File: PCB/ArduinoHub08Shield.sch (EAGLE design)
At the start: 2 parts

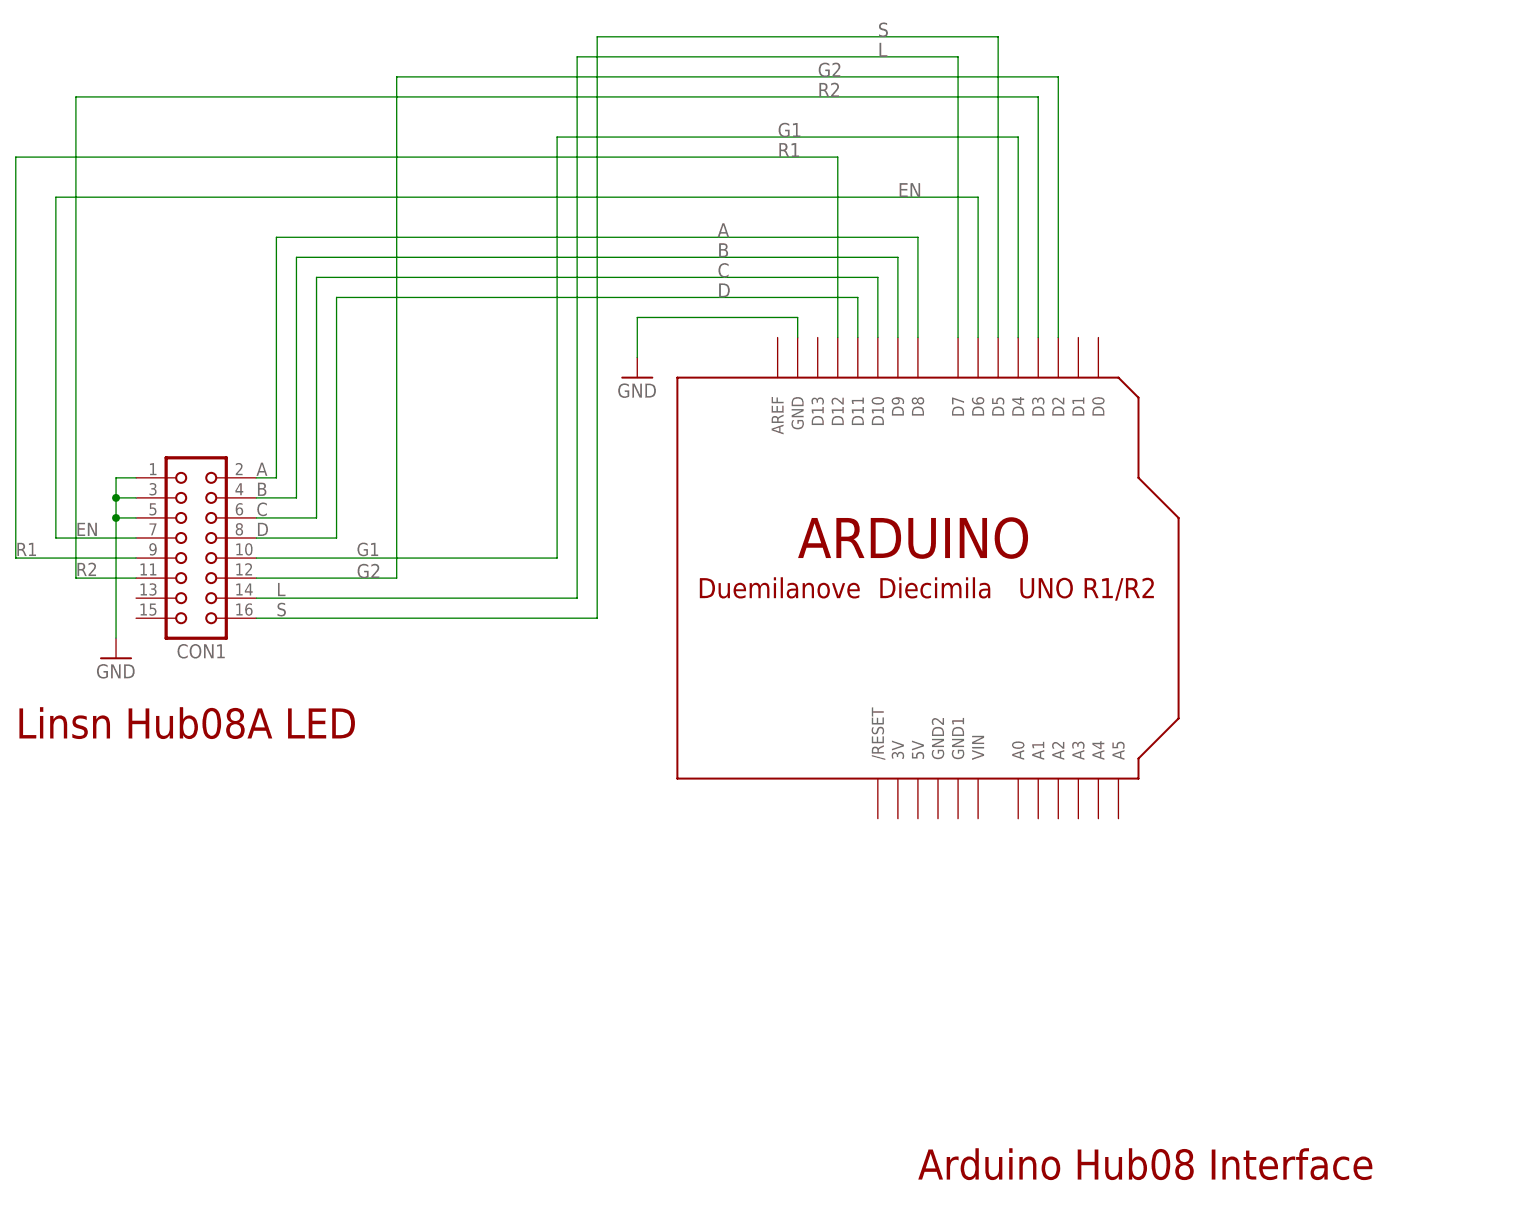
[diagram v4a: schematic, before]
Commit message: PCB/schematic update: LDR light sensor added
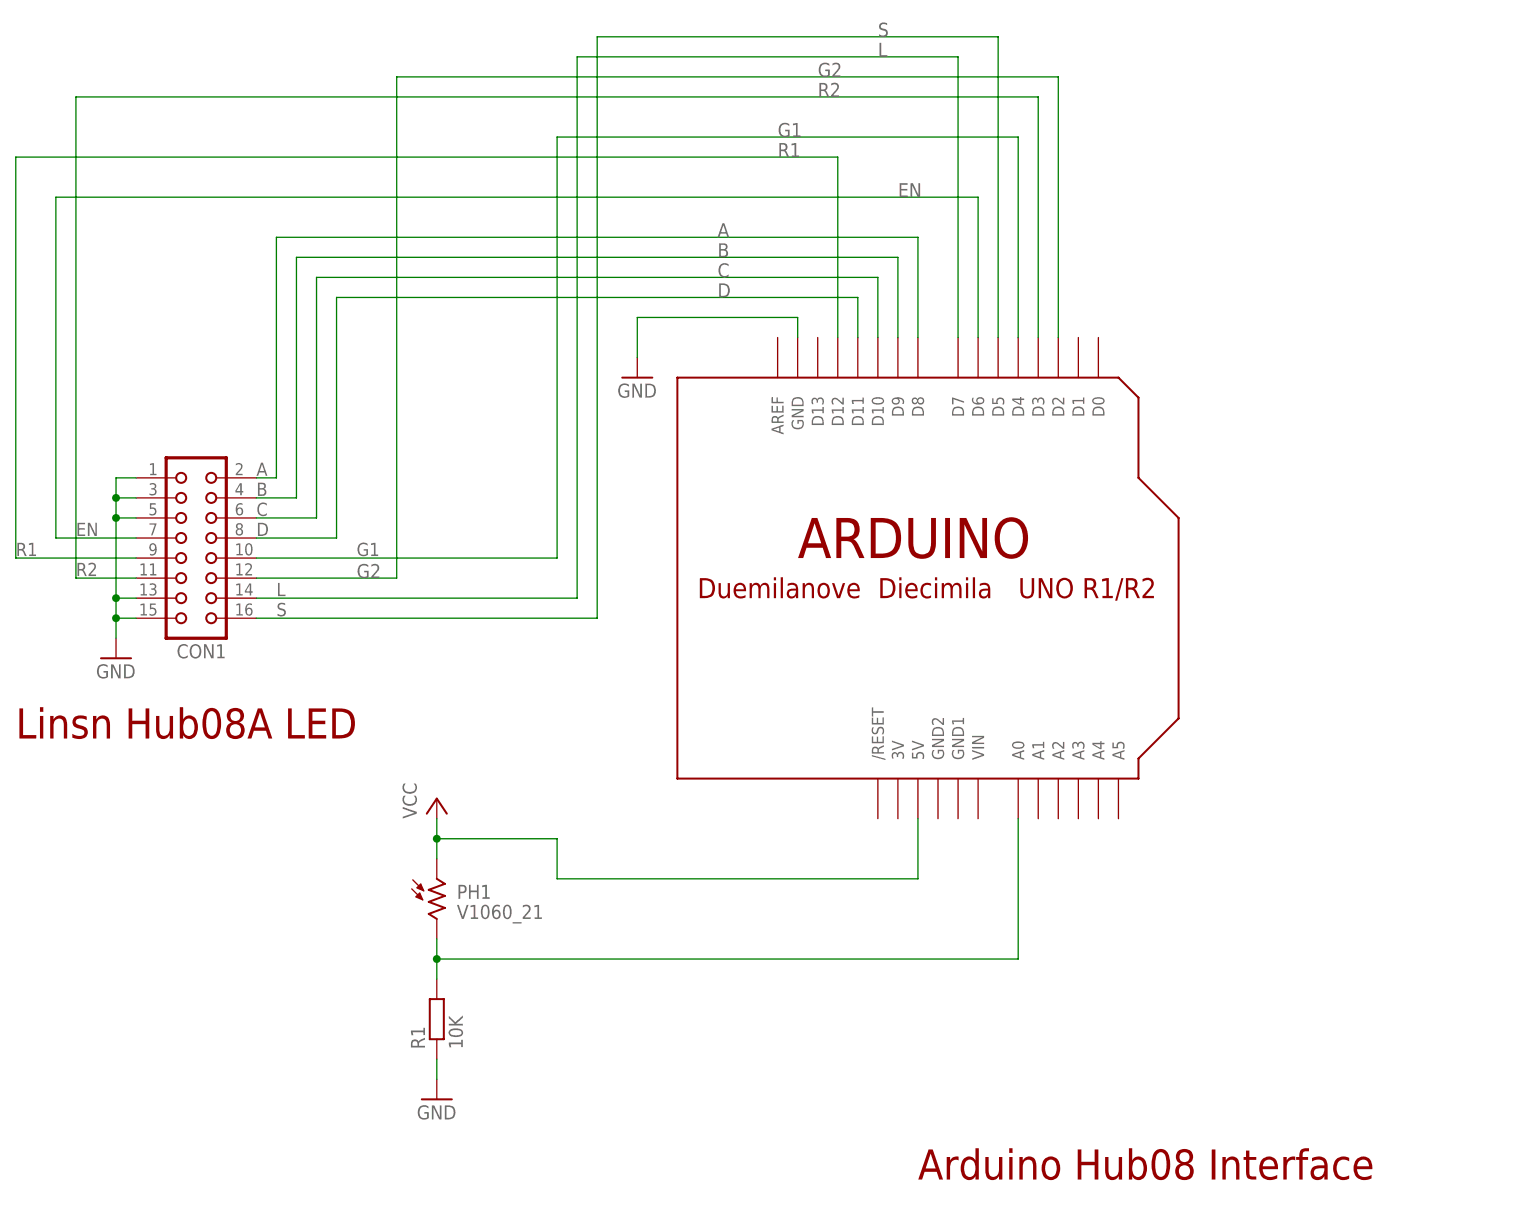
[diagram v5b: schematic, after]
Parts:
- added PH1: V1060_21, photo-elements:V1060_21
- added R1: 10K, rcl:R-EU_0204/7
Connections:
- new net N$1: PH1.2, R1.2, U$1.A0
- new net VCC: PH1.1, U$1.5V
- net GND: now also CON1.13, CON1.15, R1.1
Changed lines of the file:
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@@
 <grid distance="0.1" unitdist="inch" unit="inch" style="lines" multiple="1" display="no" altdistance="0.01" altunitdist="inch" altunit="inch"/>
 <layers>
-<layer number="1" name="Top" color="4" fill="1" visible="no" active="no"/>
-<layer number="16" name="Bottom" color="1" fill="1" visible="no" active="no"/>
-<layer number="17" name="Pads" color="2" fill="1" visible="no" active="no"/>
-<layer number="18" name="Vias" color="2" fill="1" visible="no" active="no"/>
-<layer number="19" name="Unrouted" color="6" fill="1" visible="no" active="no"/>
-<layer number="20" name="Dimension" color="15" fill="1" visible="no" active="no"/>
-<layer number="21" name="tPlace" color="7" fill="1" visible="no" active="no"/>
-<layer number="22" name="bPlace" color="7" fill="1" visible="no" active="no"/>
-<layer number="23" name="tOrigins" color="15" fill="1" visible="no" active="no"/>
-<layer number="24" name="bOrigins" color="15" fill="1" visible="no" active="no"/>
-<layer number="25" name="tNames" color="7" fill="1" visible="no" active="no"/>
-<layer number="26" name="bNames" color="7" fill="1" visible="no" active="no"/>
-<layer number="27" name="tValues" color="7" fill="1" visible="no" active="no"/>
-<layer number="28" name="bValues" color="7" fill="1" visible="no" active="no"/>
+<layer number="1" name="Top" color="4" fill="1" visible="yes" active="no"/>
+<layer number="16" name="Bottom" color="1" fill="1" visible="yes" active="no"/>
+<layer number="17" name="Pads" color="2" fill="1" visible="yes" active="no"/>
+<layer number="18" name="Vias" color="2" fill="1" visible="yes" active="no"/>
+<layer number="19" name="Unrouted" color="6" fill="1" visible="yes" active="no"/>
+<layer number="20" name="Dimension" color="15" fill="1" visible="yes" active="no"/>
+<layer number="21" name="tPlace" color="7" fill="1" visible="yes" active="no"/>
+<layer number="22" name="bPlace" color="7" fill="1" visible="yes" active="no"/>
+<layer number="23" name="tOrigins" color="15" fill="1" visible="yes" active="no"/>
+<layer number="24" name="bOrigins" color="15" fill="1" visible="yes" active="no"/>
+<layer number="25" name="tNames" color="7" fill="1" visible="yes" active="no"/>
+<layer number="26" name="bNames" color="7" fill="1" visible="yes" active="no"/>
+<layer number="27" name="tValues" color="7" fill="1" visible="yes" active="no"/>
+<layer number="28" name="bValues" color="7" fill="1" visible="yes" active="no"/>
 <layer number="29" name="tStop" color="7" fill="3" visible="no" active="no"/>
 <layer number="30" name="bStop" color="7" fill="6" visible="no" active="no"/>
@@
 <layer number="35" name="tGlue" color="7" fill="4" visible="no" active="no"/>
 <layer number="36" name="bGlue" color="7" fill="5" visible="no" active="no"/>
-<layer number="37" name="tTest" color="7" fill="1" visible="no" active="no"/>
-<layer number="38" name="bTest" color="7" fill="1" visible="no" active="no"/>
+<layer number="37" name="tTest" color="7" fill="1" visible="yes" active="no"/>
+<layer number="38" name="bTest" color="7" fill="1" visible="yes" active="no"/>
 <layer number="39" name="tKeepout" color="4" fill="11" visible="no" active="no"/>
 <layer number="40" name="bKeepout" color="1" fill="11" visible="no" active="no"/>
@@
 <layer number="44" name="Drills" color="7" fill="1" visible="no" active="no"/>
 <layer number="45" name="Holes" color="7" fill="1" visible="no" active="no"/>
-<layer number="46" name="Milling" color="3" fill="1" visible="no" active="no"/>
-<layer number="47" name="Measures" color="7" fill="1" visible="no" active="no"/>
-<layer number="48" name="Document" color="7" fill="1" visible="no" active="no"/>
-<layer number="49" name="Reference" color="7" fill="1" visible="no" active="no"/>
-<layer number="50" name="dxf" color="7" fill="1" visible="no" active="no"/>
-<layer number="51" name="tDocu" color="7" fill="1" visible="no" active="no"/>
-<layer number="52" name="bDocu" color="7" fill="1" visible="no" active="no"/>
-<layer number="53" name="tGND_GNDA" color="7" fill="9" visible="no" active="no"/>
-<layer number="54" name="bGND_GNDA" color="1" fill="9" visible="no" active="no"/>
-<layer number="56" name="wert" color="7" fill="1" visible="no" active="no"/>
-<layer number="57" name="tCAD" color="7" fill="1" visible="no" active="no"/>
+<layer number="46" name="Milling" color="3" fill="1" visible="yes" active="no"/>
+<layer number="47" name="Measures" color="7" fill="1" visible="yes" active="no"/>
+<layer number="48" name="Document" color="7" fill="1" visible="yes" active="no"/>
+<layer number="49" name="Reference" color="7" fill="1" visible="yes" active="no"/>
+<layer number="50" name="dxf" color="7" fill="1" visible="yes" active="no"/>
+<layer number="51" name="tDocu" color="7" fill="1" visible="yes" active="no"/>
+<layer number="52" name="bDocu" color="7" fill="1" visible="yes" active="no"/>
+<layer number="53" name="tGND_GNDA" color="7" fill="9" visible="yes" active="no"/>
+<layer number="54" name="bGND_GNDA" color="1" fill="9" visible="yes" active="no"/>
+<layer number="56" name="wert" color="7" fill="1" visible="yes" active="no"/>
+<layer number="57" name="tCAD" color="7" fill="1" visible="yes" active="no"/>
 <layer number="90" name="Modules" color="5" fill="1" visible="yes" active="yes"/>
 <layer number="91" name="Nets" color="2" fill="1" visible="yes" active="yes"/>
@@
 <part name="GND1" library="supply1" deviceset="GND" device=""/>
 <part name="GND2" library="supply1" deviceset="GND" device=""/>
+<part name="GND3" library="supply1" deviceset="GND" device=""/>
+<part name="P+1" library="supply1" deviceset="VCC" device=""/>
+<part name="R1" library="rcl" deviceset="R-EU_" device="0204/7" value="10K"/>
+<part name="PH1" library="photo-elements" deviceset="?1060*" device="V" technology="_21"/>
 </parts>
 <sheets>
@@
 <instance part="GND1" gate="1" x="73.66" y="93.98"/>
 <instance part="GND2" gate="1" x="139.7" y="129.54"/>
+<instance part="GND3" gate="1" x="114.3" y="38.1"/>
+<instance part="P+1" gate="VCC" x="114.3" y="76.2"/>
+<instance part="R1" gate="G$1" x="114.3" y="48.26" rot="R90"/>
+<instance part="PH1" gate="G$1" x="114.3" y="63.5"/>
 </instances>
 <busses>
@@
 <pinref part="GND1" gate="1" pin="GND"/>
 <pinref part="CON1" gate="G$1" pin="1"/>
-<wire x1="73.66" y1="96.52" x2="73.66" y2="111.76" width="0.1524" layer="91"/>
+<wire x1="73.66" y1="96.52" x2="73.66" y2="99.06" width="0.1524" layer="91"/>
+<wire x1="73.66" y1="99.06" x2="73.66" y2="101.6" width="0.1524" layer="91"/>
+<wire x1="73.66" y1="101.6" x2="73.66" y2="111.76" width="0.1524" layer="91"/>
 <wire x1="73.66" y1="111.76" x2="73.66" y2="114.3" width="0.1524" layer="91"/>
 <wire x1="73.66" y1="114.3" x2="73.66" y2="116.84" width="0.1524" layer="91"/>
@@
 <wire x1="73.66" y1="111.76" x2="76.2" y2="111.76" width="0.1524" layer="91"/>
 <junction x="73.66" y="111.76"/>
+<pinref part="CON1" gate="G$1" pin="13"/>
+<wire x1="73.66" y1="101.6" x2="76.2" y2="101.6" width="0.1524" layer="91"/>
+<junction x="73.66" y="101.6"/>
+<pinref part="CON1" gate="G$1" pin="15"/>
+<wire x1="73.66" y1="99.06" x2="76.2" y2="99.06" width="0.1524" layer="91"/>
+<junction x="73.66" y="99.06"/>
 </segment>
 <segment>
@@
 <pinref part="U$1" gate="G$1" pin="GND"/>
 <wire x1="160.02" y1="137.16" x2="160.02" y2="134.62" width="0.1524" layer="91"/>
+</segment>
+<segment>
+<pinref part="GND3" gate="1" pin="GND"/>
+<wire x1="114.3" y1="43.18" x2="114.3" y2="40.64" width="0.1524" layer="91"/>
+<pinref part="R1" gate="G$1" pin="1"/>
 </segment>
 </net>
@@
 </segment>
 </net>
+<net name="N$1" class="0">
+<segment>
+<wire x1="114.3" y1="58.42" x2="114.3" y2="55.88" width="0.1524" layer="91"/>
+<pinref part="U$1" gate="G$1" pin="A0"/>
+<wire x1="114.3" y1="55.88" x2="114.3" y2="53.34" width="0.1524" layer="91"/>
+<wire x1="114.3" y1="55.88" x2="187.96" y2="55.88" width="0.1524" layer="91"/>
+<wire x1="187.96" y1="55.88" x2="187.96" y2="73.66" width="0.1524" layer="91"/>
+<junction x="114.3" y="55.88"/>
+<pinref part="R1" gate="G$1" pin="2"/>
+<pinref part="PH1" gate="G$1" pin="2"/>
+</segment>
+</net>
+<net name="VCC" class="0">
+<segment>
+<pinref part="P+1" gate="VCC" pin="VCC"/>
+<wire x1="114.3" y1="73.66" x2="114.3" y2="71.12" width="0.1524" layer="91"/>
+<pinref part="U$1" gate="G$1" pin="5V"/>
+<wire x1="114.3" y1="71.12" x2="114.3" y2="68.58" width="0.1524" layer="91"/>
+<wire x1="175.26" y1="73.66" x2="175.26" y2="66.04" width="0.1524" layer="91"/>
+<wire x1="175.26" y1="66.04" x2="129.54" y2="66.04" width="0.1524" layer="91"/>
+<wire x1="129.54" y1="66.04" x2="129.54" y2="71.12" width="0.1524" layer="91"/>
+<wire x1="129.54" y1="71.12" x2="114.3" y2="71.12" width="0.1524" layer="91"/>
+<junction x="114.3" y="71.12"/>
+<pinref part="PH1" gate="G$1" pin="1"/>
+</segment>
+</net>
